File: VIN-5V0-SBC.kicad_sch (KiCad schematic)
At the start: 23 parts, among them U1 SW3526

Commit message: 暂存: 基本完成原理图(未分配封装，未ERC)
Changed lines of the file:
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@@
+	(wire
+		(pts
+			(xy 96.52 76.2) (xy 114.3 76.2)
+		)
+		(stroke
+			(width 0)
+			(type default)
+		)
+	)
 	(wire
 		(pts
@@
 		(pts
 			(xy 101.6 53.34) (xy 102.87 53.34)
+		)
+		(stroke
+			(width 0)
+			(type default)
+		)
+	)
+	(wire
+		(pts
+			(xy 96.52 72.39) (xy 114.3 72.39)
 		)
 		(stroke
@@
 		)
 	)
+	(label "GND"
+		(at 96.52 76.2 0)
+		(effects
+			(font
+				(size 1.27 1.27)
+			)
+			(justify left bottom)
+		)
+	)
 	(label "USB_DP"
 		(at 139.7 88.9 0)
@@
 		)
 	)
+	(label "V_{power}"
+		(at 96.52 72.39 0)
+		(effects
+			(font
+				(size 1.27 1.27)
+				(thickness 0.1588)
+			)
+			(justify left bottom)
+		)
+	)
 	(label "DP"
 		(at 33.02 40.64 0)
@@
 		)
 	)
+	(global_label "V_{power}"
+		(shape input)
+		(at 114.3 72.39 0)
+		(fields_autoplaced yes)
+		(effects
+			(font
+				(size 1.27 1.27)
+			)
+			(justify left)
+		)
+		(property "Intersheetrefs" "${INTERSHEET_REFS}"
+			(at 122.8273 72.39 0)
+			(effects
+				(font
+					(size 1.27 1.27)
+				)
+				(justify left)
+				(hide yes)
+			)
+		)
+	)
+	(global_label "GND"
+		(shape input)
+		(at 114.3 76.2 0)
+		(fields_autoplaced yes)
+		(effects
+			(font
+				(size 1.27 1.27)
+			)
+			(justify left)
+		)
+		(property "Intersheetrefs" "${INTERSHEET_REFS}"
+			(at 121.1557 76.2 0)
+			(effects
+				(font
+					(size 1.27 1.27)
+				)
+				(justify left)
+				(hide yes)
+			)
+		)
+	)

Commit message: 暂存: 基本完成原理图(差雷达接口)
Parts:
- C49: renamed from C8; footprint (none) -> Capacitor_SMD:CP_Elec_6.3x7.7
- C50: renamed from C56; footprint (none) -> Capacitor_SMD:CP_Elec_6.3x7.7
- C51: renamed from C11; footprint (none) -> Capacitor_SMD:CP_Elec_4x5.4
- C52: renamed from C59; footprint (none) -> Capacitor_SMD:CP_Elec_6.3x7.7
- C53: renamed from C12; footprint (none) -> Capacitor_SMD:C_0603_1608Metric
- C54: renamed from C57; footprint (none) -> Capacitor_SMD:CP_Elec_5x5.4
- C55: renamed from C13; footprint (none) -> Capacitor_SMD:C_0603_1608Metric
- C56: renamed from C55; footprint (none) -> Capacitor_SMD:C_0603_1608Metric
- C57: renamed from C58; footprint (none) -> Capacitor_SMD:C_0603_1608Metric
- C58: renamed from C54; footprint (none) -> Capacitor_SMD:C_0603_1608Metric
- C59: renamed from C9; footprint (none) -> Capacitor_SMD:C_0402_1005Metric
- C60: renamed from C10; footprint (none) -> Capacitor_SMD:C_0402_1005Metric
- D7: renamed from D8; footprint (none) -> LED_SMD:LED_0402_1005Metric
- D8: renamed from D9; footprint (none) -> LED_SMD:LED_0402_1005Metric
- L4: renamed from L1; footprint (none) -> Inductor_SMD:L_APV_APH1040
- R22: renamed from R5; footprint (none) -> Resistor_SMD:R_0402_1005Metric
- R23: renamed from R6; footprint (none) -> Resistor_SMD:R_0805_2012Metric
- R24: renamed from R7; footprint (none) -> Resistor_SMD:R_0402_1005Metric
- R25: renamed from R8; footprint (none) -> Resistor_SMD:R_0402_1005Metric
- renumbered D7 to D10, D1 to D9, U1 to U12

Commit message: 暂存: 布局布线基本完成(DRC未过，GND不全)
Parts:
- C52: renamed from C53; footprint Capacitor_SMD:C_0603_1608Metric -> Capacitor_SMD:C_0402_1005Metric
- C54: renamed from C55; footprint Capacitor_SMD:C_0603_1608Metric -> Capacitor_SMD:C_0402_1005Metric
- C55: renamed from C56; footprint Capacitor_SMD:C_0603_1608Metric -> Capacitor_SMD:C_0402_1005Metric
- C56: renamed from C57; footprint Capacitor_SMD:C_0603_1608Metric -> Capacitor_SMD:C_0402_1005Metric
- C57: renamed from C58; footprint Capacitor_SMD:C_0603_1608Metric -> Capacitor_SMD:C_0402_1005Metric
- renumbered C49 to C48, C50 to C49, C51 to C50, C52 to C51, C54 to C53, C59 to C58, C60 to C59
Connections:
- net DN is gone; now on net USB_DN: U12.21 (DM), USB2.5 (DN2), USB2.7 (DN1)
- net DP is gone; now on net USB_DP: U12.20 (DP), USB2.6 (DP1), USB2.8 (DP2)
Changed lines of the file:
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@@
-		)
-	)
-	(label "DP"
-		(at 137.16 52.07 0)
-		(effects
-			(font
-				(size 1.27 1.27)
-			)
-			(justify left bottom)
 		)
 	)
@@
 		)
 	)
-	(label "DN"
-		(at 137.16 49.53 0)
-		(effects
-			(font
-				(size 1.27 1.27)
-			)
-			(justify left bottom)
-		)
-	)
 	(label "GND"
 		(at 172.72 100.33 180)
@@
 		)
 	)
-	(label "DN"
-		(at 137.16 54.61 0)
-		(effects
-			(font
-				(size 1.27 1.27)
-			)
-			(justify left bottom)
-		)
-	)
 	(label "VDRV"
 		(at 88.9 99.06 0)
@@
 		)
 	)
+	(label "USB_DP"
+		(at 33.02 40.64 0)
+		(effects
+			(font
+				(size 1.27 1.27)
+			)
+			(justify left bottom)
+		)
+	)
 	(label "GND"
 		(at 96.52 76.2 0)
@@
 		)
 	)
+	(label "USB_DN"
+		(at 137.16 49.53 0)
+		(effects
+			(font
+				(size 1.27 1.27)
+			)
+			(justify left bottom)
+		)
+	)
 	(label "CC2"
 		(at 33.02 38.1 0)
@@
 		)
 	)
+	(label "USB_DN"
+		(at 33.02 43.18 0)
+		(effects
+			(font
+				(size 1.27 1.27)
+			)
+			(justify left bottom)
+		)
+	)
 	(label "V_{power}"
 		(at 20.32 90.17 0)
@@
 		)
 	)
+	(label "USB_DP"
+		(at 137.16 52.07 0)
+		(effects
+			(font
+				(size 1.27 1.27)
+			)
+			(justify left bottom)
+		)
+	)
 	(label "CC2"
 		(at 137.16 62.23 0)
@@
 		)
 	)
-	(label "DP"
-		(at 33.02 40.64 0)
+	(label "USB_DN"
+		(at 137.16 54.61 0)
 		(effects
 			(font
@@
 		)
 	)
-	(label "DP"
+	(label "USB_DP"
 		(at 137.16 57.15 0)
 		(effects
@@
 	(label "GND"
 		(at 20.32 110.49 0)
-		(effects
-			(font
-				(size 1.27 1.27)
-			)
-			(justify left bottom)
-		)
-	)
-	(label "DN"
-		(at 33.02 43.18 0)
 		(effects
 			(font
@@
 		(on_board yes)
 		(dnp no)
-		(property "Reference" "C59"
+		(property "Reference" "C58"
 			(at 153.416 99.06 90)
 			(effects
@@
 			(project "ZW1S"
 				(path "/c658c753-a869-4eb9-a520-6b2e7fae7fd9/9517e653-294f-4743-9b8d-25bbdad54970/c27468e6-6ebd-4289-8aac-6b17aa204025"
-					(reference "C59")
+					(reference "C58")
 					(unit 1)
 				)
@@
 		(on_board yes)
 		(dnp no)
-		(property "Reference" "C60"
+		(property "Reference" "C59"
 			(at 153.416 105.41 90)
 			(effects
@@
 			(project "ZW1S"
 				(path "/c658c753-a869-4eb9-a520-6b2e7fae7fd9/9517e653-294f-4743-9b8d-25bbdad54970/c27468e6-6ebd-4289-8aac-6b17aa204025"
-					(reference "C60")
+					(reference "C59")
 					(unit 1)
 				)
@@
 		(dnp no)
 		(fields_autoplaced yes)
-		(property "Reference" "C57"
+		(property "Reference" "C56"
 			(at 80.01 105.4162 0)
 			(effects
@@
 			)
 		)
-		(property "Footprint" "Capacitor_SMD:C_0603_1608Metric"
+		(property "Footprint" "Capacitor_SMD:C_0402_1005Metric"
 			(at 77.47 106.68 0)
 			(effects
@@
 			(project "ZW1S"
 				(path "/c658c753-a869-4eb9-a520-6b2e7fae7fd9/9517e653-294f-4743-9b8d-25bbdad54970/c27468e6-6ebd-4289-8aac-6b17aa204025"
-					(reference "C57")
+					(reference "C56")
 					(unit 1)
 				)
@@
 		(on_board yes)
 		(dnp no)
-		(property "Reference" "C58"
+		(property "Reference" "C57"
 			(at 99.06 48.768 90)
 			(effects
@@
 			)
 		)
-		(property "Footprint" "Capacitor_SMD:C_0603_1608Metric"
+		(property "Footprint" "Capacitor_SMD:C_0402_1005Metric"
 			(at 99.06 53.34 0)
 			(effects
@@
 			(project "ZW1S"
 				(path "/c658c753-a869-4eb9-a520-6b2e7fae7fd9/9517e653-294f-4743-9b8d-25bbdad54970/c27468e6-6ebd-4289-8aac-6b17aa204025"
-					(reference "C58")
+					(reference "C57")
 					(unit 1)
 				)
@@
 		(dnp no)
 		(fields_autoplaced yes)
-		(property "Reference" "C49"
+		(property "Reference" "C48"
 			(at 30.48 92.1638 0)
 			(effects
@@
 			(project "ZW1S"
 				(path "/c658c753-a869-4eb9-a520-6b2e7fae7fd9/9517e653-294f-4743-9b8d-25bbdad54970/c27468e6-6ebd-4289-8aac-6b17aa204025"
-					(reference "C49")
+					(reference "C48")
 					(unit 1)
 				)
@@
 		(dnp no)
 		(fields_autoplaced yes)
-		(property "Reference" "C53"
+		(property "Reference" "C52"
 			(at 63.5 92.7162 0)
 			(effects
@@
 			)
 		)
-		(property "Footprint" "Capacitor_SMD:C_0603_1608Metric"
+		(property "Footprint" "Capacitor_SMD:C_0402_1005Metric"
 			(at 60.96 93.98 0)
 			(effects
@@
 			(project "ZW1S"
 				(path "/c658c753-a869-4eb9-a520-6b2e7fae7fd9/9517e653-294f-4743-9b8d-25bbdad54970/c27468e6-6ebd-4289-8aac-6b17aa204025"
-					(reference "C53")
+					(reference "C52")
 					(unit 1)
 				)
@@
 		(dnp no)
 		(fields_autoplaced yes)
-		(property "Reference" "C50"
+		(property "Reference" "C49"
 			(at 30.48 104.8638 0)
 			(effects
@@
 			(project "ZW1S"
 				(path "/c658c753-a869-4eb9-a520-6b2e7fae7fd9/9517e653-294f-4743-9b8d-25bbdad54970/c27468e6-6ebd-4289-8aac-6b17aa204025"
-					(reference "C50")
+					(reference "C49")
 					(unit 1)
 				)
@@
 		(on_board yes)
 		(dnp no)
-		(property "Reference" "C55"
+		(property "Reference" "C54"
 			(at 76.2 37.338 0)
 			(effects
@@
 			)
 		)
-		(property "Footprint" "Capacitor_SMD:C_0603_1608Metric"
+		(property "Footprint" "Capacitor_SMD:C_0402_1005Metric"
 			(at 76.2 43.18 0)
 			(effects
@@
 			(project "ZW1S"
 				(path "/c658c753-a869-4eb9-a520-6b2e7fae7fd9/9517e653-294f-4743-9b8d-25bbdad54970/c27468e6-6ebd-4289-8aac-6b17aa204025"
-					(reference "C55")
+					(reference "C54")
 					(unit 1)
 				)
@@
 		(dnp no)
 		(fields_autoplaced yes)
-		(property "Reference" "C52"
+		(property "Reference" "C51"
 			(at 46.99 104.8638 0)
 			(effects
@@
 			(project "ZW1S"
 				(path "/c658c753-a869-4eb9-a520-6b2e7fae7fd9/9517e653-294f-4743-9b8d-25bbdad54970/c27468e6-6ebd-4289-8aac-6b17aa204025"
-					(reference "C52")
+					(reference "C51")
 					(unit 1)
 				)
@@
 		(dnp no)
 		(fields_autoplaced yes)
-		(property "Reference" "C56"
+		(property "Reference" "C55"
 			(at 80.01 92.7162 0)
 			(effects
@@
 			)
 		)
-		(property "Footprint" "Capacitor_SMD:C_0603_1608Metric"
+		(property "Footprint" "Capacitor_SMD:C_0402_1005Metric"
 			(at 77.47 93.98 0)
 			(effects
@@
 			(project "ZW1S"
 				(path "/c658c753-a869-4eb9-a520-6b2e7fae7fd9/9517e653-294f-4743-9b8d-25bbdad54970/c27468e6-6ebd-4289-8aac-6b17aa204025"
-					(reference "C56")
+					(reference "C55")
 					(unit 1)
 				)
@@
 		(dnp no)
 		(fields_autoplaced yes)
-		(property "Reference" "C51"
+		(property "Reference" "C50"
 			(at 46.99 92.7162 0)
 			(effects
@@
 			(project "ZW1S"
 				(path "/c658c753-a869-4eb9-a520-6b2e7fae7fd9/9517e653-294f-4743-9b8d-25bbdad54970/c27468e6-6ebd-4289-8aac-6b17aa204025"
-					(reference "C51")
+					(reference "C50")
 					(unit 1)
 				)
@@
 		(dnp no)
 		(fields_autoplaced yes)
-		(property "Reference" "C54"
+		(property "Reference" "C53"
 			(at 63.5 105.4162 0)
 			(effects
@@
 			(project "ZW1S"
 				(path "/c658c753-a869-4eb9-a520-6b2e7fae7fd9/9517e653-294f-4743-9b8d-25bbdad54970/c27468e6-6ebd-4289-8aac-6b17aa204025"
-					(reference "C54")
-					(unit 1)
-				)
+					(reference "C53")
+					(unit 1)
+				)

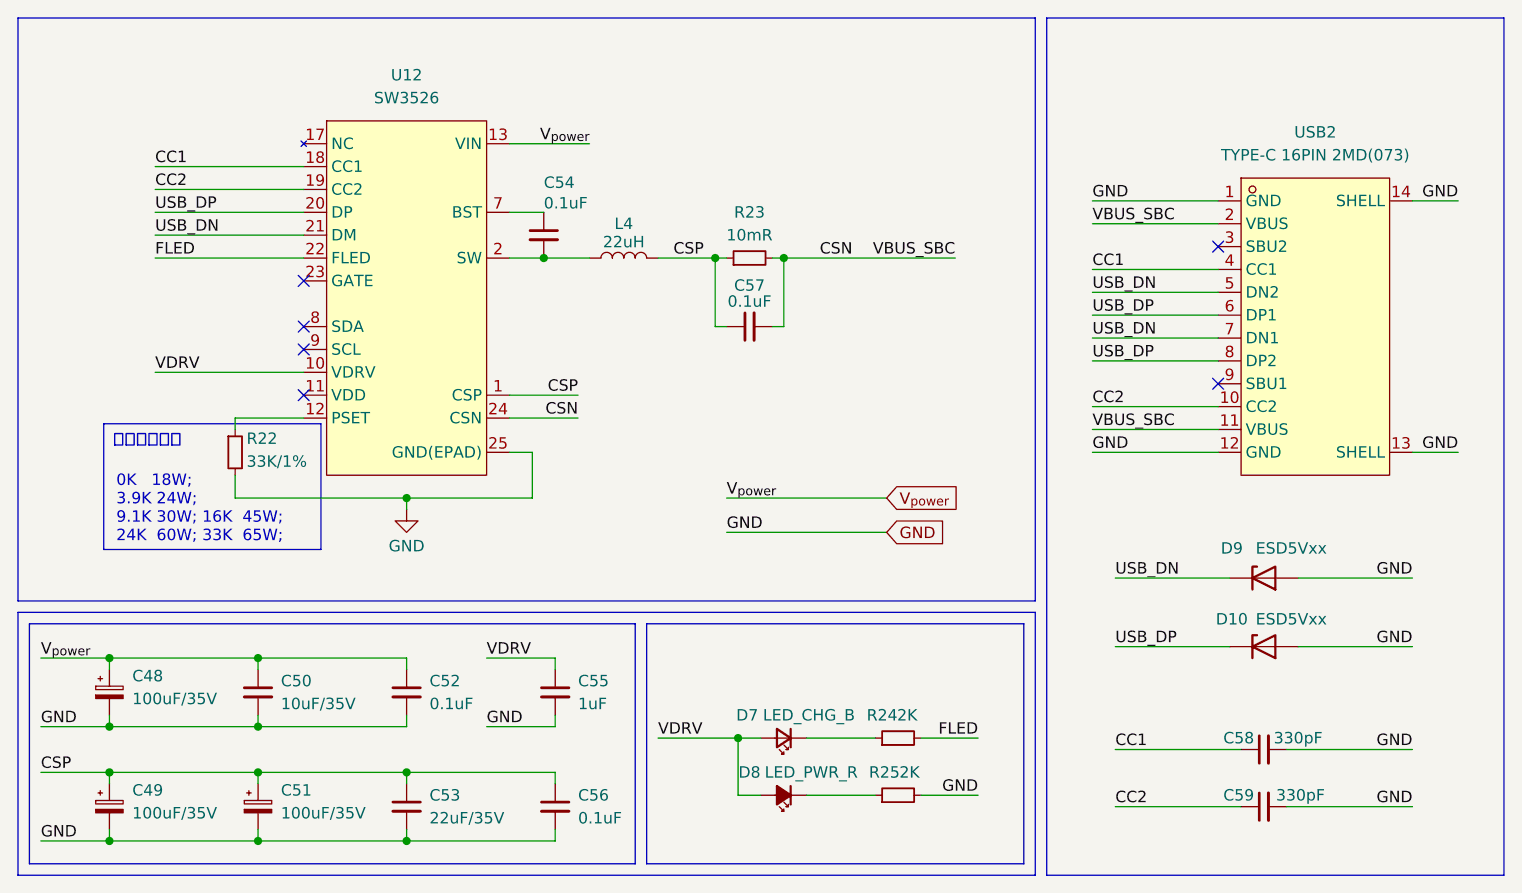
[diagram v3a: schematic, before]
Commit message: pref: USB外设改自供电，优化布线
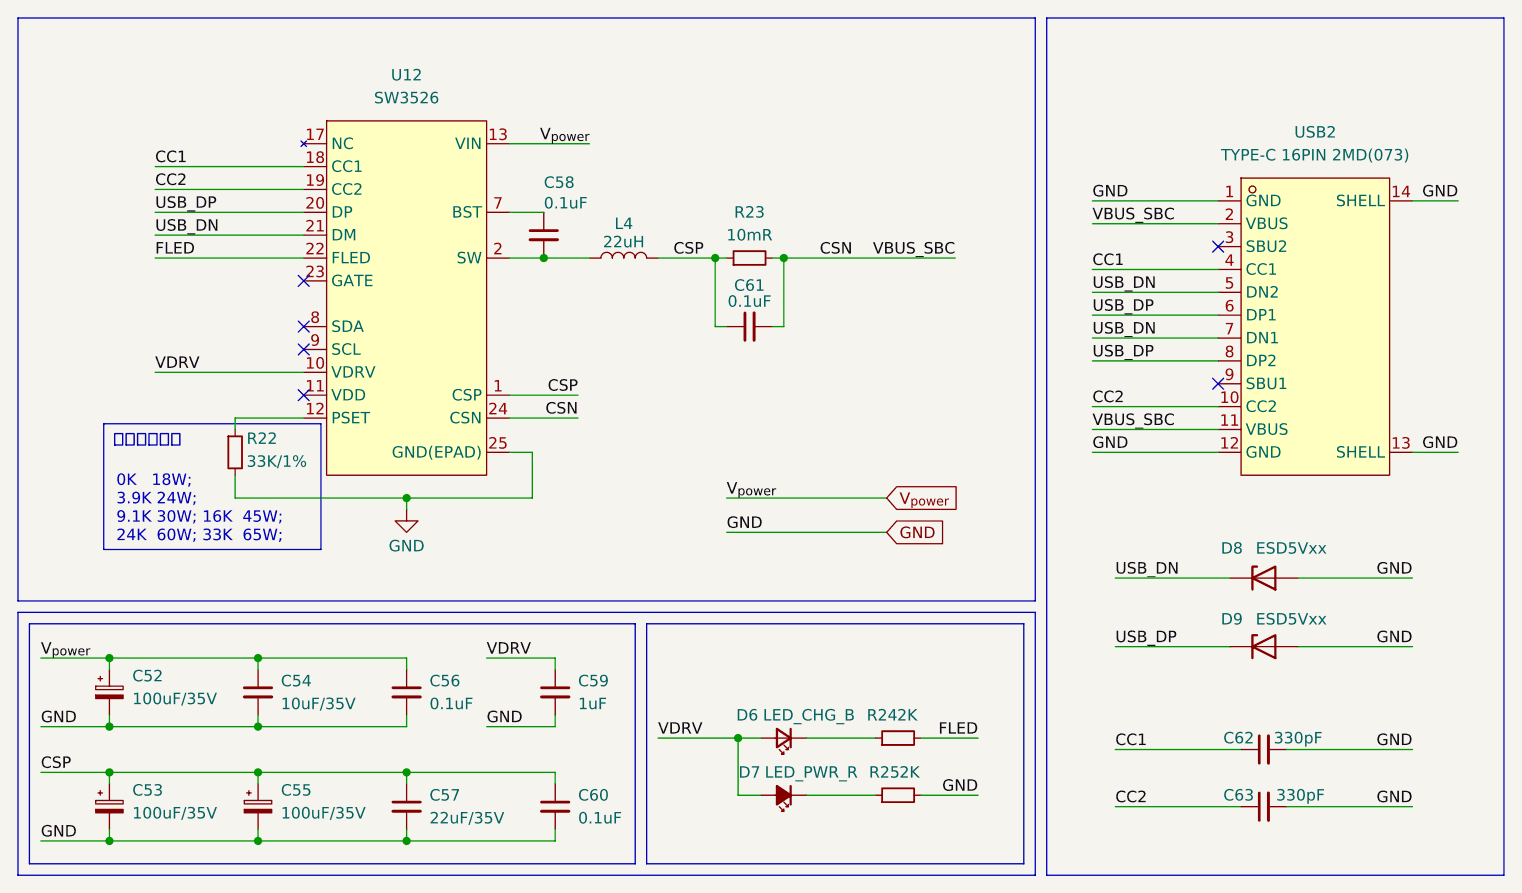
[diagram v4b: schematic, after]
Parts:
- renumbered C48 to C52, C49 to C53, C50 to C54, C51 to C55, C52 to C56, C53 to C57, C54 to C58, C55 to C59, C56 to C60, C57 to C61, C58 to C62, C59 to C63, D7 to D6, D8 to D7, D9 to D8, D10 to D9
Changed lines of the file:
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@@
 		(on_board yes)
 		(dnp no)
-		(property "Reference" "C58"
+		(property "Reference" "C62"
 			(at 153.416 99.06 90)
 			(effects
@@
 			(project "ZW1S"
 				(path "/c658c753-a869-4eb9-a520-6b2e7fae7fd9/9517e653-294f-4743-9b8d-25bbdad54970/c27468e6-6ebd-4289-8aac-6b17aa204025"
-					(reference "C58")
+					(reference "C62")
 					(unit 1)
 				)
@@
 		(on_board yes)
 		(dnp no)
-		(property "Reference" "C59"
+		(property "Reference" "C63"
 			(at 153.416 105.41 90)
 			(effects
@@
 			(project "ZW1S"
 				(path "/c658c753-a869-4eb9-a520-6b2e7fae7fd9/9517e653-294f-4743-9b8d-25bbdad54970/c27468e6-6ebd-4289-8aac-6b17aa204025"
-					(reference "C59")
+					(reference "C63")
 					(unit 1)
 				)
@@
 		(on_board yes)
 		(dnp no)
-		(property "Reference" "D8"
+		(property "Reference" "D7"
 			(at 99.06 102.87 0)
 			(effects
@@
 			(project "ZW1S"
 				(path "/c658c753-a869-4eb9-a520-6b2e7fae7fd9/9517e653-294f-4743-9b8d-25bbdad54970/c27468e6-6ebd-4289-8aac-6b17aa204025"
-					(reference "D8")
+					(reference "D7")
 					(unit 1)
 				)
@@
 		(dnp no)
 		(fields_autoplaced yes)
-		(property "Reference" "C56"
+		(property "Reference" "C60"
 			(at 80.01 105.4162 0)
 			(effects
@@
 			(project "ZW1S"
 				(path "/c658c753-a869-4eb9-a520-6b2e7fae7fd9/9517e653-294f-4743-9b8d-25bbdad54970/c27468e6-6ebd-4289-8aac-6b17aa204025"
-					(reference "C56")
+					(reference "C60")
 					(unit 1)
 				)
@@
 		(on_board yes)
 		(dnp no)
-		(property "Reference" "D9"
+		(property "Reference" "D8"
 			(at 152.654 77.978 0)
 			(effects
@@
 			(project "ZW1S"
 				(path "/c658c753-a869-4eb9-a520-6b2e7fae7fd9/9517e653-294f-4743-9b8d-25bbdad54970/c27468e6-6ebd-4289-8aac-6b17aa204025"
-					(reference "D9")
+					(reference "D8")
 					(unit 1)
 				)
@@
 		(on_board yes)
 		(dnp no)
-		(property "Reference" "C57"
+		(property "Reference" "C61"
 			(at 99.06 48.768 90)
 			(effects
@@
 			(project "ZW1S"
 				(path "/c658c753-a869-4eb9-a520-6b2e7fae7fd9/9517e653-294f-4743-9b8d-25bbdad54970/c27468e6-6ebd-4289-8aac-6b17aa204025"
-					(reference "C57")
+					(reference "C61")
 					(unit 1)
 				)
@@
 		(dnp no)
 		(fields_autoplaced yes)
-		(property "Reference" "C48"
+		(property "Reference" "C52"
 			(at 30.48 92.1638 0)
 			(effects
@@
 			(project "ZW1S"
 				(path "/c658c753-a869-4eb9-a520-6b2e7fae7fd9/9517e653-294f-4743-9b8d-25bbdad54970/c27468e6-6ebd-4289-8aac-6b17aa204025"
-					(reference "C48")
+					(reference "C52")
 					(unit 1)
 				)
@@
 		(dnp no)
 		(fields_autoplaced yes)
-		(property "Reference" "C52"
+		(property "Reference" "C56"
 			(at 63.5 92.7162 0)
 			(effects
@@
 			(project "ZW1S"
 				(path "/c658c753-a869-4eb9-a520-6b2e7fae7fd9/9517e653-294f-4743-9b8d-25bbdad54970/c27468e6-6ebd-4289-8aac-6b17aa204025"
-					(reference "C52")
+					(reference "C56")
 					(unit 1)
 				)
@@
 		(dnp no)
 		(fields_autoplaced yes)
-		(property "Reference" "C49"
+		(property "Reference" "C53"
 			(at 30.48 104.8638 0)
 			(effects
@@
 			(project "ZW1S"
 				(path "/c658c753-a869-4eb9-a520-6b2e7fae7fd9/9517e653-294f-4743-9b8d-25bbdad54970/c27468e6-6ebd-4289-8aac-6b17aa204025"
-					(reference "C49")
+					(reference "C53")
 					(unit 1)
 				)
@@
 		(on_board yes)
 		(dnp no)
-		(property "Reference" "#PWR12"
+		(property "Reference" "#PWR13"
 			(at 60.96 80.01 0)
 			(effects
@@
 			(project "ZW1S"
 				(path "/c658c753-a869-4eb9-a520-6b2e7fae7fd9/9517e653-294f-4743-9b8d-25bbdad54970/c27468e6-6ebd-4289-8aac-6b17aa204025"
-					(reference "#PWR12")
+					(reference "#PWR13")
 					(unit 1)
 				)
@@
 		(on_board yes)
 		(dnp no)
-		(property "Reference" "C54"
+		(property "Reference" "C58"
 			(at 76.2 37.338 0)
 			(effects
@@
 			(project "ZW1S"
 				(path "/c658c753-a869-4eb9-a520-6b2e7fae7fd9/9517e653-294f-4743-9b8d-25bbdad54970/c27468e6-6ebd-4289-8aac-6b17aa204025"
-					(reference "C54")
+					(reference "C58")
 					(unit 1)
 				)
@@
 		(dnp no)
 		(fields_autoplaced yes)
-		(property "Reference" "C51"
+		(property "Reference" "C55"
 			(at 46.99 104.8638 0)
 			(effects
@@
 			(project "ZW1S"
 				(path "/c658c753-a869-4eb9-a520-6b2e7fae7fd9/9517e653-294f-4743-9b8d-25bbdad54970/c27468e6-6ebd-4289-8aac-6b17aa204025"
-					(reference "C51")
+					(reference "C55")
 					(unit 1)
 				)
@@
 		(on_board yes)
 		(dnp no)
-		(property "Reference" "D7"
+		(property "Reference" "D6"
 			(at 98.806 96.52 0)
 			(effects
@@
 			(project ""
 				(path "/c658c753-a869-4eb9-a520-6b2e7fae7fd9/9517e653-294f-4743-9b8d-25bbdad54970/c27468e6-6ebd-4289-8aac-6b17aa204025"
-					(reference "D7")
+					(reference "D6")
 					(unit 1)
 				)
@@
 		(dnp no)
 		(fields_autoplaced yes)
-		(property "Reference" "C55"
+		(property "Reference" "C59"
 			(at 80.01 92.7162 0)
 			(effects
@@
 			(project "ZW1S"
 				(path "/c658c753-a869-4eb9-a520-6b2e7fae7fd9/9517e653-294f-4743-9b8d-25bbdad54970/c27468e6-6ebd-4289-8aac-6b17aa204025"
-					(reference "C55")
+					(reference "C59")
 					(unit 1)
 				)
@@
 		(dnp no)
 		(fields_autoplaced yes)
-		(property "Reference" "C50"
+		(property "Reference" "C54"
 			(at 46.99 92.7162 0)
 			(effects
@@
 			(project "ZW1S"
 				(path "/c658c753-a869-4eb9-a520-6b2e7fae7fd9/9517e653-294f-4743-9b8d-25bbdad54970/c27468e6-6ebd-4289-8aac-6b17aa204025"
-					(reference "C50")
+					(reference "C54")
 					(unit 1)
 				)
@@
 		(on_board yes)
 		(dnp no)
-		(property "Reference" "D10"
+		(property "Reference" "D9"
 			(at 152.654 85.852 0)
 			(effects
@@
 			(project "ZW1S"
 				(path "/c658c753-a869-4eb9-a520-6b2e7fae7fd9/9517e653-294f-4743-9b8d-25bbdad54970/c27468e6-6ebd-4289-8aac-6b17aa204025"
-					(reference "D10")
+					(reference "D9")
 					(unit 1)
 				)
@@
 		(dnp no)
 		(fields_autoplaced yes)
-		(property "Reference" "C53"
+		(property "Reference" "C57"
 			(at 63.5 105.4162 0)
 			(effects
@@
 			(project "ZW1S"
 				(path "/c658c753-a869-4eb9-a520-6b2e7fae7fd9/9517e653-294f-4743-9b8d-25bbdad54970/c27468e6-6ebd-4289-8aac-6b17aa204025"
-					(reference "C53")
-					(unit 1)
-				)
+					(reference "C57")
+					(unit 1)
+				)
